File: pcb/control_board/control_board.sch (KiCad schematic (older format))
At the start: 47 parts, among them J1 Barrel_Jack, J2 Conn_01x24_Female, J3 Conn_01x24_Female, J4 Conn_02x06_Top_Bottom, SW1 SW_Push, SW2 SW_Push, SW3 SW_Push, SW4 SW_Push, SW5 SW_Push, SW6 SW_Push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

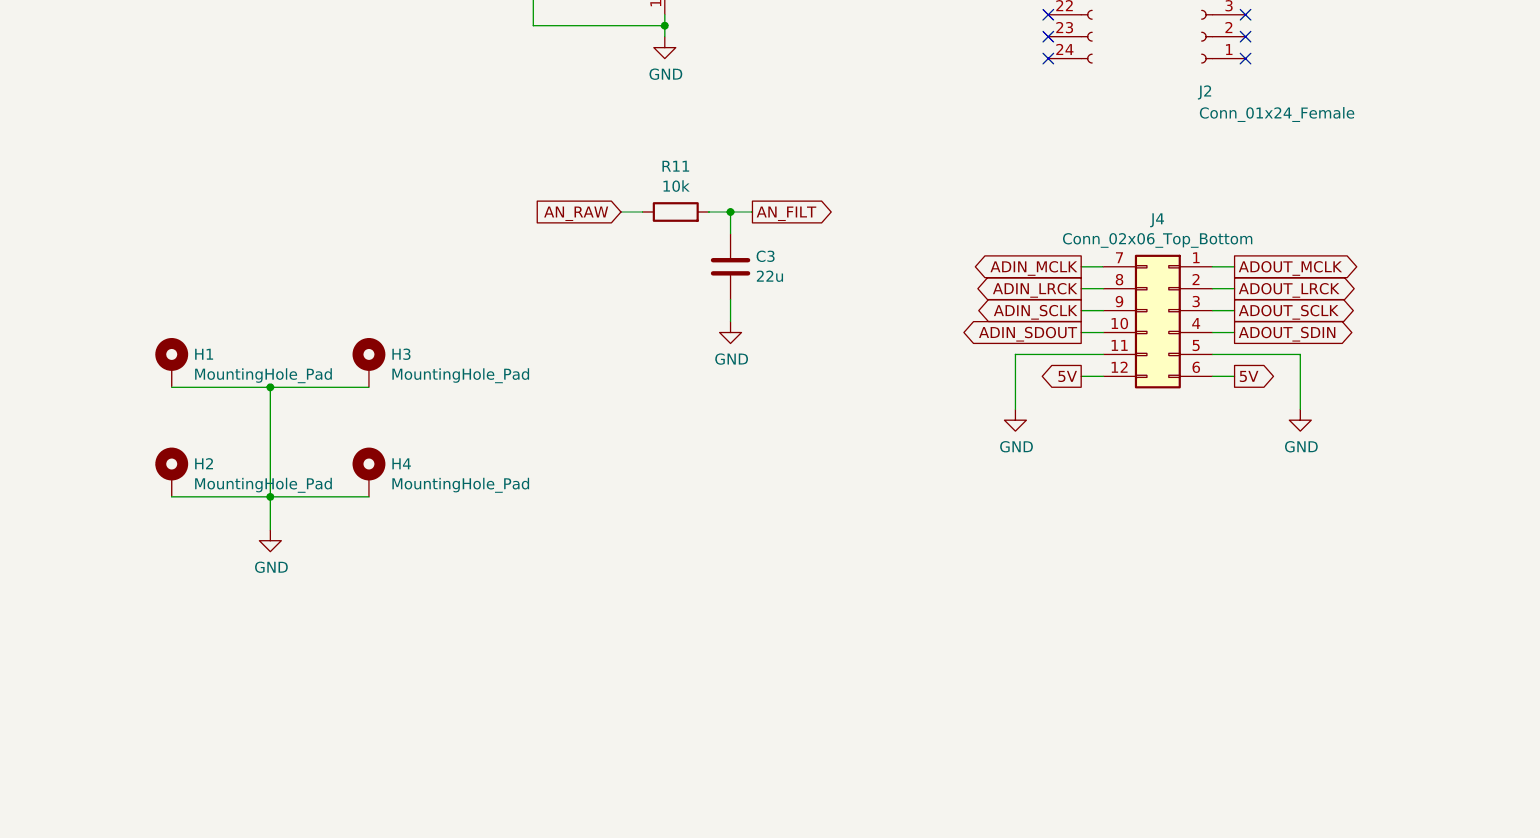
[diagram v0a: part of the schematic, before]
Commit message: Correctly place CMOD headers, add divider to filter to drop potentiometer voltage into range of CMOD ADC.
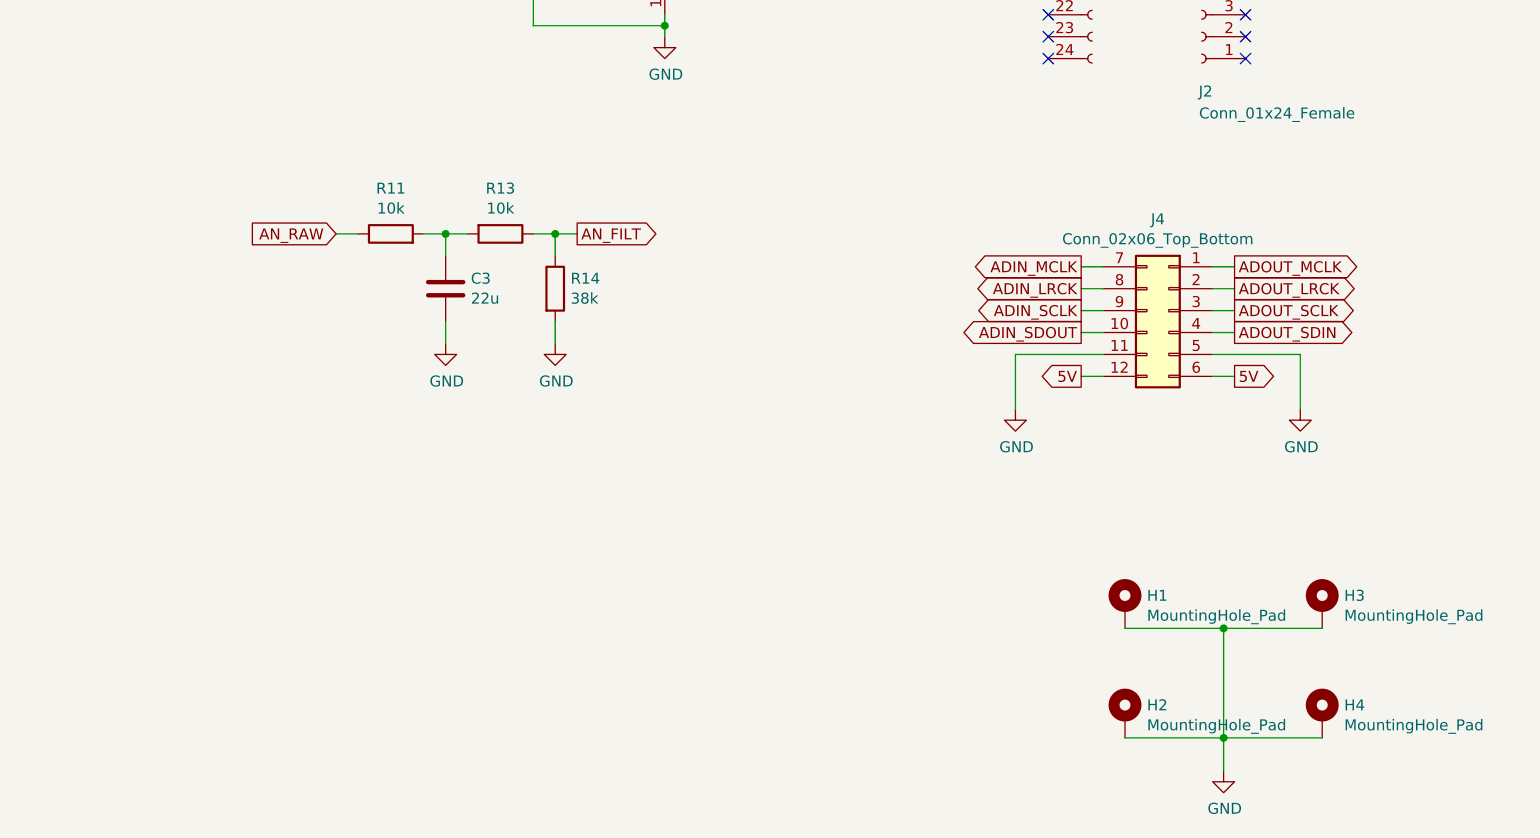
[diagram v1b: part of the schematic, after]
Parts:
- added R13: 10k, Resistor_SMD:R_0805_2012Metric_Pad1.15x1.40mm_HandSolder, symbol Device:R
- added R14: 38k, Resistor_SMD:R_0805_2012Metric_Pad1.15x1.40mm_HandSolder, symbol Device:R
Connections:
- net AN_FILT: now also R13.1, R14.1; no longer C3.1, R11.2
- net GND: now also R14.2
- new net: C3.1, R11.2, R13.2
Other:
- moved on the sheet: C3, H1, H2, H3, H4, R11
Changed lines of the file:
@@
 L Device:C C3
 U 1 1 5CF69F2F
-P 12150 4350
-F 0 "C3" H 12265 4396 50  0000 L CNN
-F 1 "22u" H 12265 4305 50  0000 L CNN
-F 2 "Capacitor_SMD:C_0805_2012Metric_Pad1.15x1.40mm_HandSolder" H 12188 4200 50  0001 C CNN
-F 3 "~" H 12150 4350 50  0001 C CNN
-	1    12150 4350
+P 10850 4450
+F 0 "C3" H 10965 4496 50  0000 L CNN
+F 1 "22u" H 10965 4405 50  0000 L CNN
+F 2 "Capacitor_SMD:C_0805_2012Metric_Pad1.15x1.40mm_HandSolder" H 10888 4300 50  0001 C CNN
+F 3 "~" H 10850 4450 50  0001 C CNN
+	1    10850 4450
 	1    0    0    -1
 $EndComp
@@
 L Device:R R11
 U 1 1 5CF6A591
-P 11900 4100
-F 0 "R11" V 12107 4100 50  0000 C CNN
-F 1 "10k" V 12016 4100 50  0000 C CNN
-F 2 "Resistor_SMD:R_0805_2012Metric_Pad1.15x1.40mm_HandSolder" V 11830 4100 50  0001 C CNN
-F 3 "~" H 11900 4100 50  0001 C CNN
-	1    11900 4100
+P 10600 4200
+F 0 "R11" V 10807 4200 50  0000 C CNN
+F 1 "10k" V 10716 4200 50  0000 C CNN
+F 2 "Resistor_SMD:R_0805_2012Metric_Pad1.15x1.40mm_HandSolder" V 10530 4200 50  0001 C CNN
+F 3 "~" H 10600 4200 50  0001 C CNN
+	1    10600 4200
 	0    -1   -1   0
 $EndComp
@@
 L power:GND #PWR0130
 U 1 1 5CF6AE53
-P 12150 4600
-F 0 "#PWR0130" H 12150 4350 50  0001 C CNN
-F 1 "GND" H 12155 4427 50  0000 C CNN
-F 2 "" H 12150 4600 50  0001 C CNN
-F 3 "" H 12150 4600 50  0001 C CNN
-	1    12150 4600
-	1    0    0    -1
-$EndComp
-Wire Wire Line
-	12050 4100 12150 4100
-Wire Wire Line
-	12150 4100 12150 4200
-Wire Wire Line
-	12150 4500 12150 4600
-Wire Wire Line
-	11650 4100 11750 4100
-Text GLabel 11650 4100 0    50   Input ~ 0
+P 10850 4700
+F 0 "#PWR0130" H 10850 4450 50  0001 C CNN
+F 1 "GND" H 10855 4527 50  0000 C CNN
+F 2 "" H 10850 4700 50  0001 C CNN
+F 3 "" H 10850 4700 50  0001 C CNN
+	1    10850 4700
+	1    0    0    -1
+$EndComp
+Wire Wire Line
+	10750 4200 10850 4200
+Wire Wire Line
+	10850 4200 10850 4300
+Wire Wire Line
+	10850 4600 10850 4700
+Wire Wire Line
+	10350 4200 10450 4200
+Text GLabel 10350 4200 0    50   Input ~ 0
 AN_RAW
 Wire Wire Line
-	12250 4100 12150 4100
-Connection ~ 12150 4100
-Text GLabel 12250 4100 2    50   Output ~ 0
+	10950 4200 10850 4200
+Connection ~ 10850 4200
+Text GLabel 11450 4200 2    50   Output ~ 0
 AN_FILT
 Wire Wire Line
@@
 L power:GND #PWR0134
 U 1 1 5CE6D4CD
-P 10050 5550
-F 0 "#PWR0134" H 10050 5300 50  0001 C CNN
-F 1 "GND" H 10055 5377 50  0000 C CNN
-F 2 "" H 10050 5550 50  0001 C CNN
-F 3 "" H 10050 5550 50  0001 C CNN
-	1    10050 5550
+P 14400 6650
+F 0 "#PWR0134" H 14400 6400 50  0001 C CNN
+F 1 "GND" H 14405 6477 50  0000 C CNN
+F 2 "" H 14400 6650 50  0001 C CNN
+F 3 "" H 14400 6650 50  0001 C CNN
+	1    14400 6650
 	1    0    0    -1
 $EndComp
@@
 L Mechanical:MountingHole_Pad H1
 U 1 1 5CE6EE05
-P 9600 4800
-F 0 "H1" H 9700 4849 50  0000 L CNN
-F 1 "MountingHole_Pad" H 9700 4758 50  0000 L CNN
-F 2 "MountingHole:MountingHole_2.5mm_Pad" H 9600 4800 50  0001 C CNN
-F 3 "~" H 9600 4800 50  0001 C CNN
-	1    9600 4800
+P 13950 5900
+F 0 "H1" H 14050 5949 50  0000 L CNN
+F 1 "MountingHole_Pad" H 14050 5858 50  0000 L CNN
+F 2 "MountingHole:MountingHole_2.5mm_Pad" H 13950 5900 50  0001 C CNN
+F 3 "~" H 13950 5900 50  0001 C CNN
+	1    13950 5900
 	1    0    0    -1
 $EndComp
@@
 L Mechanical:MountingHole_Pad H3
 U 1 1 5CE6FE7D
-P 10500 4800
-F 0 "H3" H 10600 4849 50  0000 L CNN
-F 1 "MountingHole_Pad" H 10600 4758 50  0000 L CNN
-F 2 "MountingHole:MountingHole_2.5mm_Pad" H 10500 4800 50  0001 C CNN
-F 3 "~" H 10500 4800 50  0001 C CNN
-	1    10500 4800
+P 14850 5900
+F 0 "H3" H 14950 5949 50  0000 L CNN
+F 1 "MountingHole_Pad" H 14950 5858 50  0000 L CNN
+F 2 "MountingHole:MountingHole_2.5mm_Pad" H 14850 5900 50  0001 C CNN
+F 3 "~" H 14850 5900 50  0001 C CNN
+	1    14850 5900
 	1    0    0    -1
 $EndComp
@@
 L Mechanical:MountingHole_Pad H4
 U 1 1 5CE70B25
-P 10500 5300
-F 0 "H4" H 10600 5349 50  0000 L CNN
-F 1 "MountingHole_Pad" H 10600 5258 50  0000 L CNN
-F 2 "MountingHole:MountingHole_2.5mm_Pad" H 10500 5300 50  0001 C CNN
-F 3 "~" H 10500 5300 50  0001 C CNN
-	1    10500 5300
+P 14850 6400
+F 0 "H4" H 14950 6449 50  0000 L CNN
+F 1 "MountingHole_Pad" H 14950 6358 50  0000 L CNN
+F 2 "MountingHole:MountingHole_2.5mm_Pad" H 14850 6400 50  0001 C CNN
+F 3 "~" H 14850 6400 50  0001 C CNN
+	1    14850 6400
 	1    0    0    -1
 $EndComp
@@
 L Mechanical:MountingHole_Pad H2
 U 1 1 5CE7171D
-P 9600 5300
-F 0 "H2" H 9700 5349 50  0000 L CNN
-F 1 "MountingHole_Pad" H 9700 5258 50  0000 L CNN
-F 2 "MountingHole:MountingHole_2.5mm_Pad" H 9600 5300 50  0001 C CNN
-F 3 "~" H 9600 5300 50  0001 C CNN
-	1    9600 5300
-	1    0    0    -1
-$EndComp
-Wire Wire Line
-	10050 5400 10050 5550
-Wire Wire Line
-	9600 5400 10050 5400
-Wire Wire Line
-	9600 4900 10050 4900
-Connection ~ 10050 5400
-Wire Wire Line
-	10050 5400 10500 5400
-Wire Wire Line
-	10050 5400 10050 4900
-Connection ~ 10050 4900
-Wire Wire Line
-	10050 4900 10500 4900
+P 13950 6400
+F 0 "H2" H 14050 6449 50  0000 L CNN
+F 1 "MountingHole_Pad" H 14050 6358 50  0000 L CNN
+F 2 "MountingHole:MountingHole_2.5mm_Pad" H 13950 6400 50  0001 C CNN
+F 3 "~" H 13950 6400 50  0001 C CNN
+	1    13950 6400
+	1    0    0    -1
+$EndComp
+Wire Wire Line
+	14400 6500 14400 6650
+Wire Wire Line
+	13950 6500 14400 6500
+Wire Wire Line
+	13950 6000 14400 6000
+Connection ~ 14400 6500
+Wire Wire Line
+	14400 6500 14850 6500
+Wire Wire Line
+	14400 6500 14400 6000
+Connection ~ 14400 6000
+Wire Wire Line
+	14400 6000 14850 6000
+$Comp
+L Device:R R13
+U 1 1 5CDCCB12
+P 11100 4200
+F 0 "R13" V 10893 4200 50  0000 C CNN
+F 1 "10k" V 10984 4200 50  0000 C CNN
+F 2 "Resistor_SMD:R_0805_2012Metric_Pad1.15x1.40mm_HandSolder" V 11030 4200 50  0001 C CNN
+F 3 "~" H 11100 4200 50  0001 C CNN
+	1    11100 4200
+	0    1    1    0
+$EndComp
+$Comp
+L Device:R R14
+U 1 1 5CDCD903
+P 11350 4450
+F 0 "R14" H 11420 4496 50  0000 L CNN
+F 1 "38k" H 11420 4405 50  0000 L CNN
+F 2 "Resistor_SMD:R_0805_2012Metric_Pad1.15x1.40mm_HandSolder" V 11280 4450 50  0001 C CNN
+F 3 "~" H 11350 4450 50  0001 C CNN
+	1    11350 4450
+	1    0    0    -1
+$EndComp
+$Comp
+L power:GND #PWR01
+U 1 1 5CDCF043
+P 11350 4700
+F 0 "#PWR01" H 11350 4450 50  0001 C CNN
+F 1 "GND" H 11355 4527 50  0000 C CNN
+F 2 "" H 11350 4700 50  0001 C CNN
+F 3 "" H 11350 4700 50  0001 C CNN
+	1    11350 4700
+	1    0    0    -1
+$EndComp
+Wire Wire Line
+	11350 4700 11350 4600
+Wire Wire Line
+	11350 4300 11350 4200
+Wire Wire Line
+	11350 4200 11250 4200
+Wire Wire Line
+	11350 4200 11450 4200
+Connection ~ 11350 4200
 $EndSCHEMATC

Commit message: Add connectors for switches rather than holes for direct wires.
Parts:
- SW1, SW2, SW3, SW4, SW5, SW6: footprint Connector_Wire:SolderWirePad_1x02_P7.62mm_Drill2.5mm -> Connector_PinHeader_2.54mm:PinHeader_2x01_P2.54mm_Vertical
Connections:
- net 5V: now also U1.9 (I0)
- no-connect marks 27 -> 26
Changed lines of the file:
@@
 F 0 "SW1" H 1250 3285 50  0000 C CNN
 F 1 "SW_Push" H 1250 3194 50  0000 C CNN
-F 2 "Connector_Wire:SolderWirePad_1x02_P7.62mm_Drill2.5mm" H 1250 3200 50  0001 C CNN
+F 2 "Connector_PinHeader_2.54mm:PinHeader_2x01_P2.54mm_Vertical" H 1250 3200 50  0001 C CNN
 F 3 "" H 1250 3200 50  0001 C CNN
 	1    1250 3000
@@
 F 0 "SW2" H 2950 3285 50  0000 C CNN
 F 1 "SW_Push" H 2950 3194 50  0000 C CNN
-F 2 "Connector_Wire:SolderWirePad_1x02_P7.62mm_Drill2.5mm" H 2950 3200 50  0001 C CNN
+F 2 "Connector_PinHeader_2.54mm:PinHeader_2x01_P2.54mm_Vertical" H 2950 3200 50  0001 C CNN
 F 3 "" H 2950 3200 50  0001 C CNN
 	1    2950 3000
@@
 F 0 "SW3" H 4500 3285 50  0000 C CNN
 F 1 "SW_Push" H 4500 3194 50  0000 C CNN
-F 2 "Connector_Wire:SolderWirePad_1x02_P7.62mm_Drill2.5mm" H 4500 3200 50  0001 C CNN
+F 2 "Connector_PinHeader_2.54mm:PinHeader_2x01_P2.54mm_Vertical" H 4500 3200 50  0001 C CNN
 F 3 "" H 4500 3200 50  0001 C CNN
 	1    4500 3000
@@
 F 0 "SW4" H 6100 3285 50  0000 C CNN
 F 1 "SW_Push" H 6100 3194 50  0000 C CNN
-F 2 "Connector_Wire:SolderWirePad_1x02_P7.62mm_Drill2.5mm" H 6100 3200 50  0001 C CNN
+F 2 "Connector_PinHeader_2.54mm:PinHeader_2x01_P2.54mm_Vertical" H 6100 3200 50  0001 C CNN
 F 3 "" H 6100 3200 50  0001 C CNN
 	1    6100 3000
@@
 F 0 "SW5" H 7700 3285 50  0000 C CNN
 F 1 "SW_Push" H 7700 3194 50  0000 C CNN
-F 2 "Connector_Wire:SolderWirePad_1x02_P7.62mm_Drill2.5mm" H 7700 3200 50  0001 C CNN
+F 2 "Connector_PinHeader_2.54mm:PinHeader_2x01_P2.54mm_Vertical" H 7700 3200 50  0001 C CNN
 F 3 "" H 7700 3200 50  0001 C CNN
 	1    7700 3000
@@
 tremolo_speed
 Wire Wire Line
-	11250 1400 11350 1400
-Wire Wire Line
 	11250 2500 11350 2500
 Wire Wire Line
@@
 Wire Wire Line
 	12450 1600 12350 1600
-NoConn ~ 11250 1400
 $Comp
 L Connector:Barrel_Jack J1
@@
 F 0 "SW6" H 3250 1535 50  0000 C CNN
 F 1 "SW_Push" H 3250 1444 50  0000 C CNN
-F 2 "Connector_Wire:SolderWirePad_1x02_P7.62mm_Drill2.5mm" H 3250 1450 50  0001 C CNN
+F 2 "Connector_PinHeader_2.54mm:PinHeader_2x01_P2.54mm_Vertical" H 3250 1450 50  0001 C CNN
 F 3 "~" H 3250 1450 50  0001 C CNN
 	1    3250 1250
@@
 	11350 4200 11450 4200
 Connection ~ 11350 4200
+Wire Wire Line
+	10950 1300 10950 1400
+Wire Wire Line
+	10950 1400 11350 1400
+Text GLabel 10950 1300 1    50   Input ~ 0
+5V
 $EndSCHEMATC
